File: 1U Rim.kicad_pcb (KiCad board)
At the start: 2 copper layers, 56.9 x 28.7 mm, 68 parts, among them J1 Trigger, J10 POT_M, J2 Accent, J3 PWR, J4 Out, J5 PWR_C, J6 PWR_M, J7 JCK_C, J8 JCK_M, J9 POT_C, Q1 BC849, Q2 BC859, Q3 BC849, U1 TL074, U2 TL072

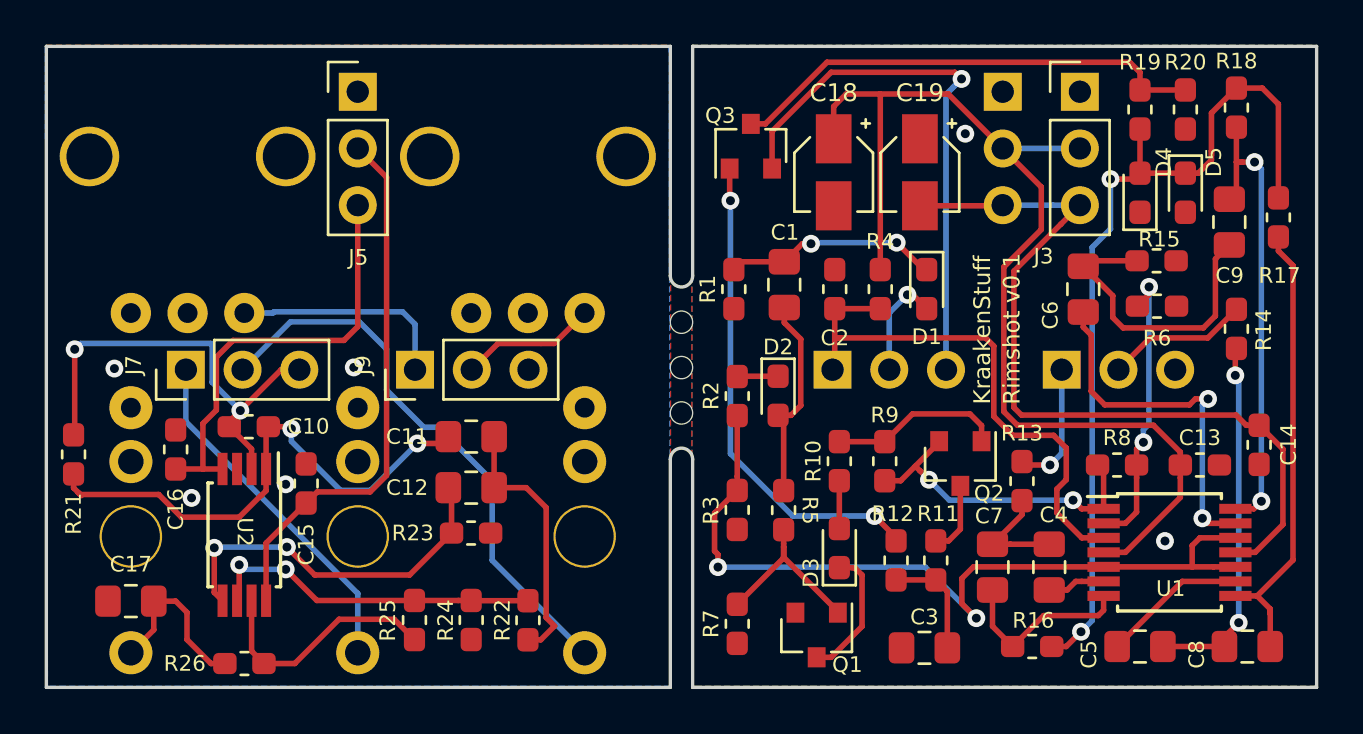
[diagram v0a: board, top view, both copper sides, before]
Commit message: Fixed three missing resistors Fixed pot orientation
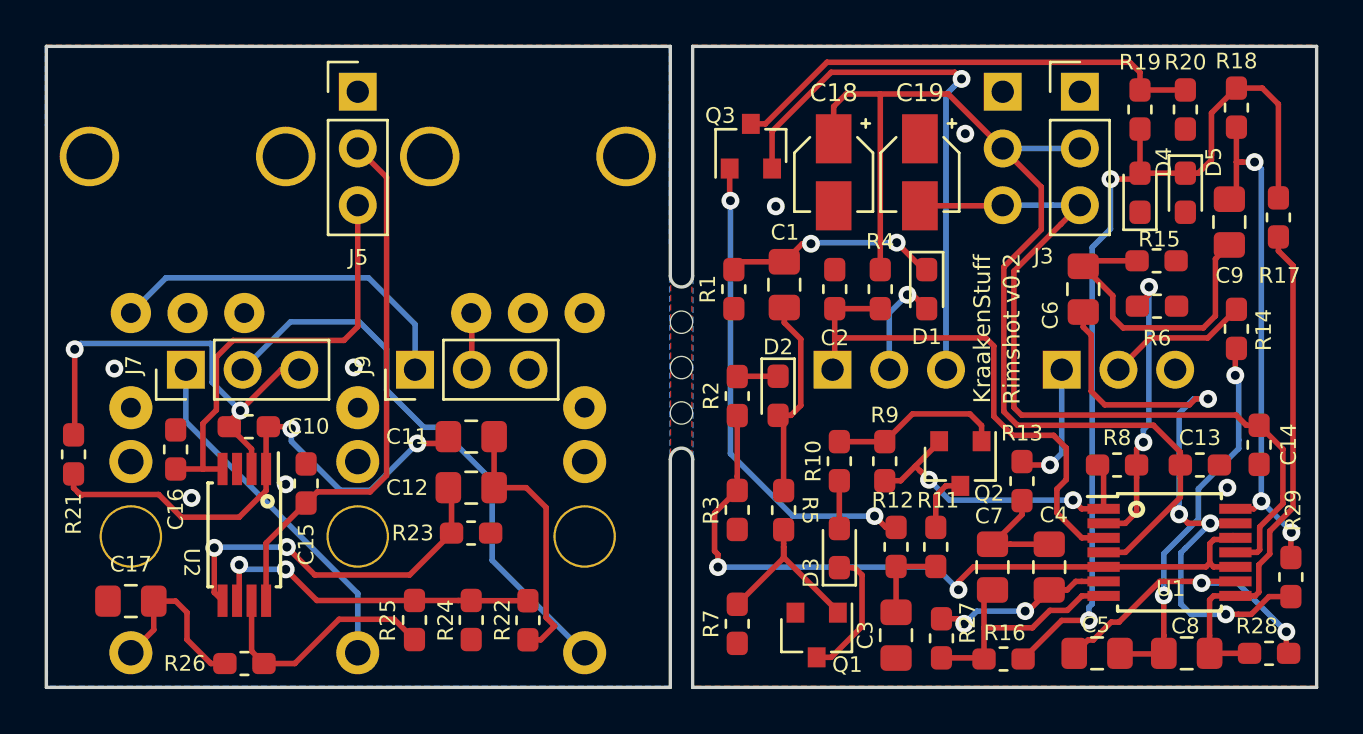
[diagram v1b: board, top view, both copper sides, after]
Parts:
- added R27: 470k, Resistor_SMD:R_0603_1608Metric_Pad1.05x0.95mm_HandSolder, F.Cu at (60.2, 48.1)
- added R28: 330k, Resistor_SMD:R_0603_1608Metric_Pad1.05x0.95mm_HandSolder, F.Cu at (74.9, 48.8)
- added R29: 470k, Resistor_SMD:R_0603_1608Metric_Pad1.05x0.95mm_HandSolder, F.Cu at (75.8, 45.4)
- R21: value 0R -> 100k
- moved C8 2.73 mm to (71.2, 48.8)
- moved C5 1.95 mm to (67.2, 48.8)
- moved R16 1.40 mm to (63.0, 49.1)
- moved C3 1.39 mm to (58.2, 48.0), turned to 270 degrees
- moved R11 0.60 mm to (59.9, 44.1)
- moved R12 0.60 mm to (58.2, 44.1)
- renumbered Tune2 to RV1, Tune1 to RV2
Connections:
- RV1 pad 1: Ptc1 -> GND
- RV1 pad 3: GND -> Ptc1
- RV2 pad 1: Ptc2 -> GND
- RV2 pad 3: GND -> Ptc2
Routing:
- net Net-(C6-Pad2): track 16.3 -> 27.9 mm, vias 2 -> 4
- net Net-(C5-Pad2): track 6.50 -> 14.4 mm, vias 0 -> 2
- net Ptc1: track 15.7 -> 22.1 mm
- net Net-(C4-Pad2): track 2.59 -> 8.14 mm, vias 0 -> 2
- net Ptc2: track 12.5 -> 8.95 mm
- net Net-(R2-Pad1): track 37.3 -> 33.9 mm
- net Net-(C9-Pad1): track 20.8 -> 24.0 mm, vias 2 -> 3
- net Net-(C7-Pad1): track 8.29 -> 11.1 mm
- net Net-(C8-Pad1): track 20.6 -> 23.3 mm
- net Net-(D4-Pad2): track 39.8 -> 41.2 mm
- net Net-(C3-Pad1): track 5.03 -> 3.83 mm
- net Net-(C5-Pad1): track 16.5 -> 17.1 mm
- net Net-(Q2-Pad3): track 3.26 -> 2.70 mm
- net GND: vias 6 -> 7
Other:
- board text added: "Rimshot v0.2"
- board text removed: "Rimshot v0.1"
